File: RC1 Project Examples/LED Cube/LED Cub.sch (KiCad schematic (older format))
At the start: 32 parts, among them J1 Signals, J5 Port A, J6 Port B, Q1 PN2222A, Q2 PN2222A, Q3 PN2222A, Q4 PN2222A, Q5 PN2222A, Q6 PN2222A, Q7 PN2222A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

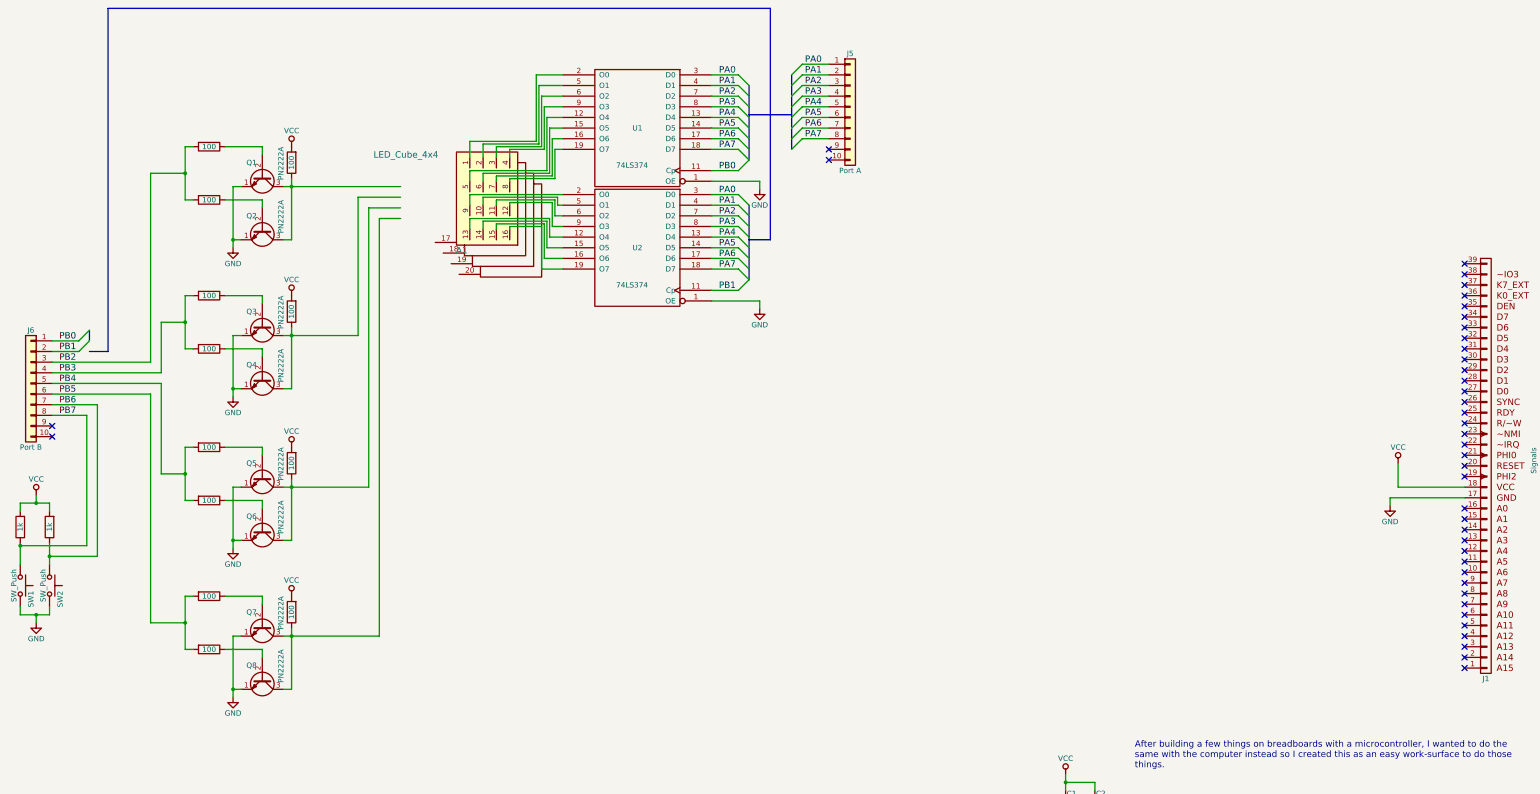
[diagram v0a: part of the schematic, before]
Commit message: LED Cube schematic updated
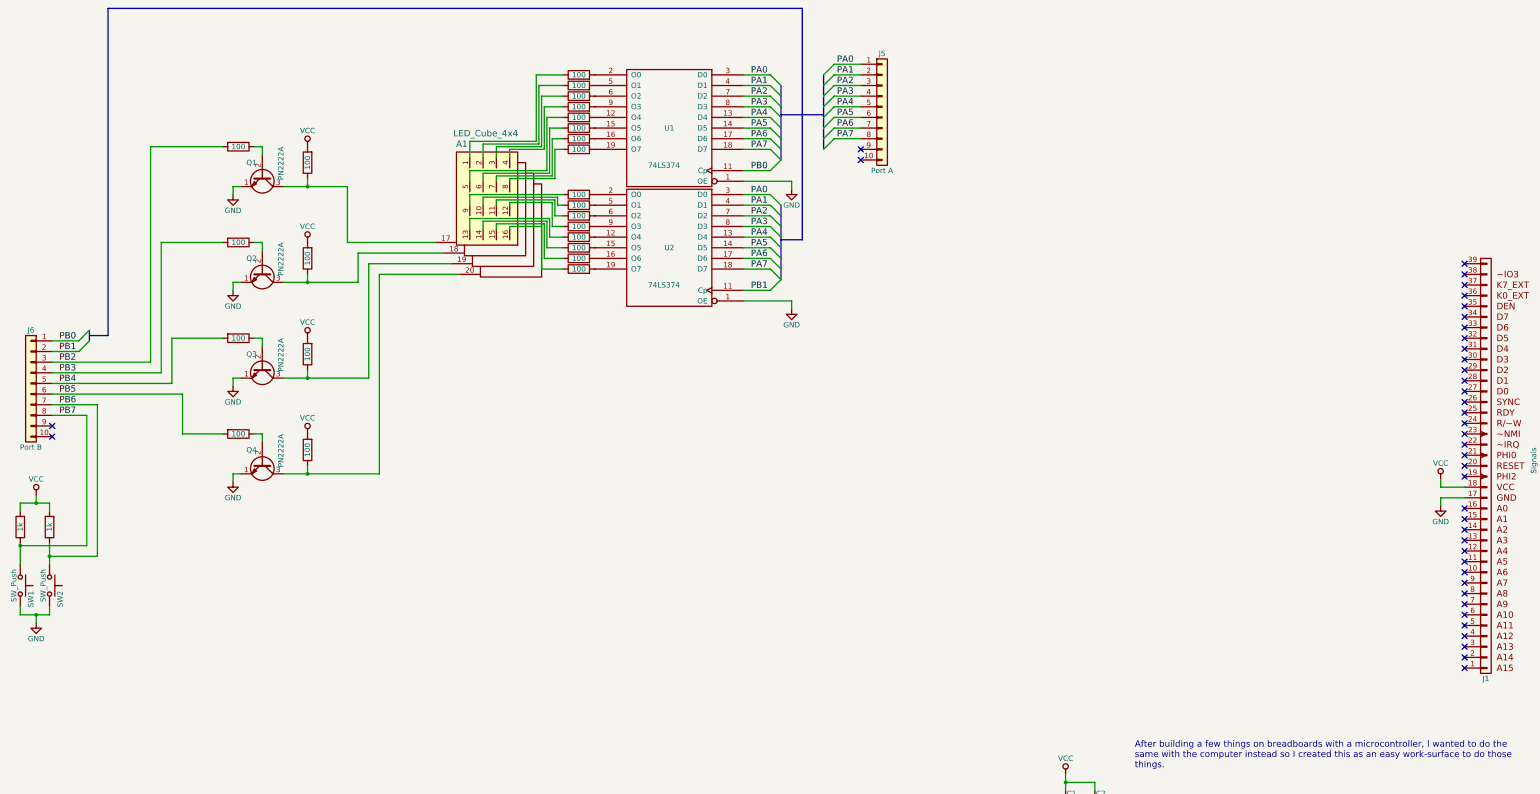
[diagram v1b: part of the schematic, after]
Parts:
- removed Q5, Q6, Q7, Q8: PN2222A, TO_SOT_Packages_THT:TO-92_Molded_Narrow, symbol PN2222A
- added R15, R16, R17, R18, R19, R20, R21, R22, R23, R24, R25, R26: 100, Resistors_THT:R_Axial_DIN0207_L6.3mm_D2.5mm_P10.16mm_Horizontal, symbol R
- A1: footprint (none) -> led_cube:LED_Cube_4x4
- R1, R10, R11, R12, R13, R14, R2, R3, R4, R5, R6, R7, R8, R9: footprint (none) -> Resistors_THT:R_Axial_DIN0207_L6.3mm_D2.5mm_P10.16mm_Horizontal
- SW1, SW2: footprint (none) -> Buttons_Switches_THT:SW_PUSH_6mm
- U1, U2: footprint (none) -> Housings_DIP:DIP-20_W7.62mm_Socket_LongPads
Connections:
- net PB2: no longer R2.2
- net PB3: now also R2.2; no longer R3.2, R4.2
- net PB4: now also R3.2; no longer R5.2, R6.2
- net PB5: now also R4.2; no longer R7.2, R8.2
- net VCC: now also R5.2, R6.2, R7.2; no longer R10.2, R11.2, R12.2
- net at A1.1 (la1): now also R8.1; no longer U1.2 (O0)
- net at A1.10 (la10): now also R20.1; no longer U2.5 (O1)
- net at A1.11 (la11): now also R21.1; no longer U2.6 (O2)
- net at A1.12 (la12): now also R22.1; no longer U2.9 (O3)
- net at A1.13 (la13): now also R23.1; no longer U2.12 (O4)
- net at A1.14 (la14): now also R24.1; no longer U2.15 (O5)
- net at A1.15 (la15): now also R25.1; no longer U2.16 (O6)
- net at A1.16 (la16): now also R26.1; no longer U2.19 (O7)
- net at A1.17 (layer0): now also Q1.3 (C), R9.1
- net at A1.18 (layer1): now also Q2.3 (C), R5.1
- net at A1.19 (layer2): now also Q3.3 (C), R6.1
- net at A1.2 (la2): now also R10.1; no longer U1.5 (O1)
- net at A1.20 (layer3): now also Q4.3 (C), R7.1
- net at A1.3 (la3): now also R11.1; no longer U1.6 (O2)
- net at A1.4 (la4): now also R12.1; no longer U1.9 (O3)
- net at A1.5 (la5): now also R15.1; no longer U1.12 (O4)
- net at A1.6 (la6): now also R16.1; no longer U1.15 (O5)
- net at A1.7 (la7): now also R17.1; no longer U1.16 (O6)
- net at A1.8 (la8): now also R18.1; no longer U1.19 (O7)
- net at A1.9 (la9): now also R19.1; no longer U2.2 (O0)
- new net: R15.2, U1.12 (O4)
- new net: R16.2, U1.15 (O5)
- new net: R17.2, U1.16 (O6)
- new net: R18.2, U1.19 (O7)
- new net: R8.2, U1.2 (O0)
- new net: R10.2, U1.5 (O1)
- new net: R11.2, U1.6 (O2)
- new net: R12.2, U1.9 (O3)
- new net: R23.2, U2.12 (O4)
- new net: R24.2, U2.15 (O5)
- new net: R25.2, U2.16 (O6)
- new net: R26.2, U2.19 (O7)
- new net: R19.2, U2.2 (O0)
- new net: R20.2, U2.5 (O1)
- new net: R21.2, U2.6 (O2)
- new net: R22.2, U2.9 (O3)
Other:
- moved on the sheet: J5, U1, U2

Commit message: Layout done
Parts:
- added M1, M2, M3: Mounting, mounting:1pin, symbol Mounting
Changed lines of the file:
@@
 	0    -1   -1   0
 $EndComp
+$Comp
+L Mounting M3
+U 1 1 5E007EB8
+P 15975 550
+F 0 "M3" H 15975 650 50  0001 C CNN
+F 1 "Mounting" H 15975 475 50  0001 C CNN
+F 2 "mounting:1pin" H 15975 550 50  0001 C CNN
+F 3 "" H 15975 550 50  0001 C CNN
+	1    15975 550
+	1    0    0    -1
+$EndComp
+$Comp
+L Mounting M2
+U 1 1 5E007F3A
+P 15850 550
+F 0 "M2" H 15850 650 50  0001 C CNN
+F 1 "Mounting" H 15850 475 50  0001 C CNN
+F 2 "mounting:1pin" H 15850 550 50  0001 C CNN
+F 3 "" H 15850 550 50  0001 C CNN
+	1    15850 550
+	1    0    0    -1
+$EndComp
+$Comp
+L Mounting M1
+U 1 1 5E007F6F
+P 15725 550
+F 0 "M1" H 15725 650 50  0001 C CNN
+F 1 "Mounting" H 15725 475 50  0001 C CNN
+F 2 "mounting:1pin" H 15725 550 50  0001 C CNN
+F 3 "" H 15725 550 50  0001 C CNN
+	1    15725 550
+	1    0    0    -1
+$EndComp
 $EndSCHEMATC
